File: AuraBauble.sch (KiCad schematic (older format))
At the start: 35 parts, among them J1 Bauble-Expando!, J2 USB_A, J3 SWD, SW1 KXT 321 LHS, U1 ATSAMD11D14A-M, U2 LP5912-3.3DRV, U3 74LVC1G02SE-7, Y1 FC-135R

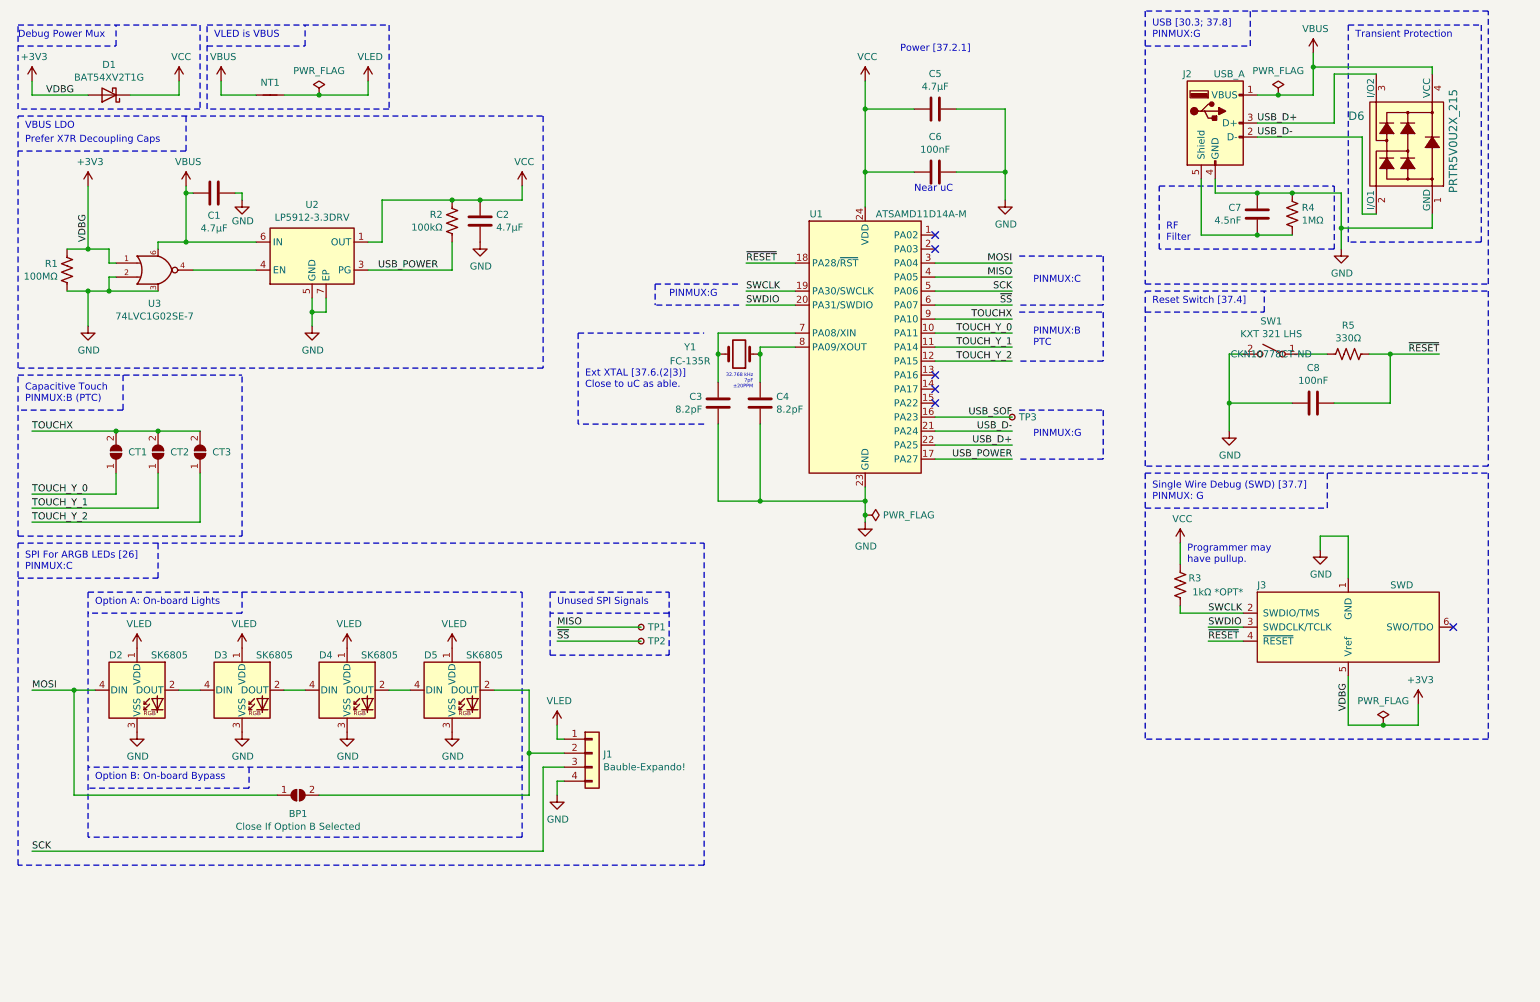
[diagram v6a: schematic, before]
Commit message: Closing in on a rev0.
I still think I need to level shift the SPI signals to the LEDs.
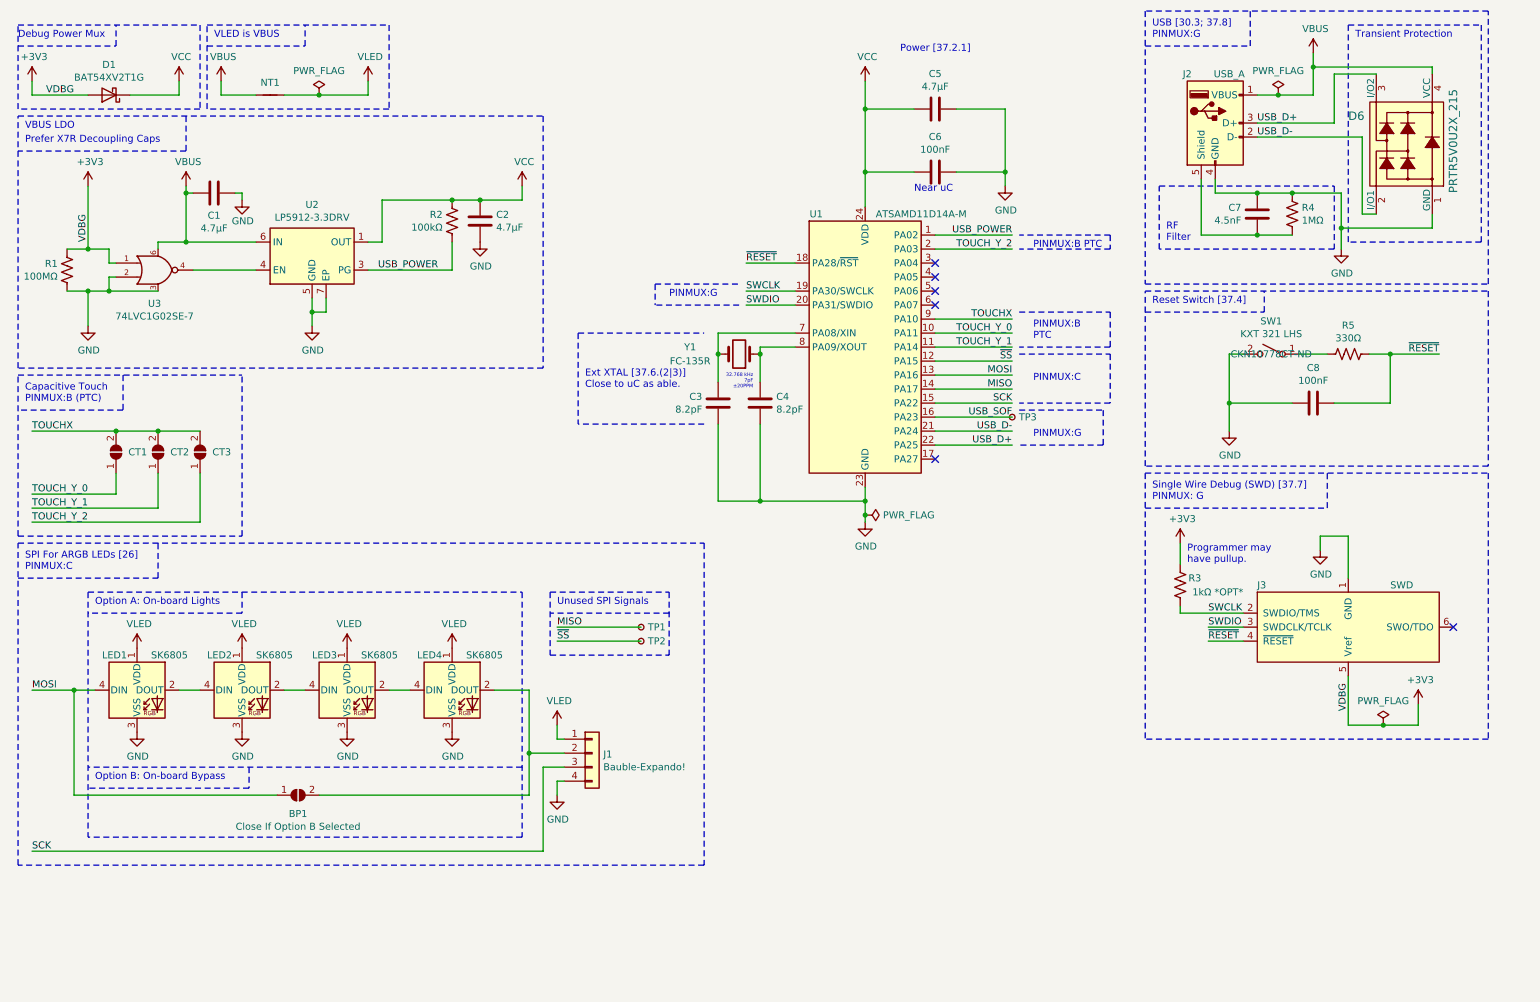
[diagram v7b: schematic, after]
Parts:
- J3: footprint Connector_DebugEdge:DebugEdge_2x05_Target -> Connector_DebugEdge:DebugEdge_2x03_Target
- renumbered D2 to LED1, D3 to LED2, D4 to LED3, D5 to LED4
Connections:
- net +3V3: now also R3.2
- net MISO: now also U1.14 (PA17); no longer U1.4 (PA05)
- net MOSI: now also U1.13 (PA16); no longer U1.3 (PA04)
- net SCK: now also U1.15 (PA22); no longer U1.5 (PA06)
- net TOUCH_Y_2: now also U1.2 (PA03); no longer U1.12 (PA15)
- net USB_POWER: now also U1.1 (PA02); no longer U1.17 (PA27)
- net VCC: no longer R3.2
- net ~SS~: now also U1.12 (PA15); no longer U1.6 (PA07)
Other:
- note added: "PINMUX:B PTC"
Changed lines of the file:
@@
 Near uC
 Wire Wire Line
-	7700 1650 7700 1850
+	7700 1650 7700 1750
 Connection ~ 7700 1650
 Wire Wire Line
@@
 L power:GND #PWR024
 U 1 1 5F5D1520
-P 7700 1850
-F 0 "#PWR024" H 7700 1600 50  0001 C CNN
-F 1 "GND" H 7705 1677 50  0000 C CNN
-F 2 "" H 7700 1850 50  0001 C CNN
-F 3 "" H 7700 1850 50  0001 C CNN
-	1    7700 1850
+P 7700 1750
+F 0 "#PWR024" H 7700 1500 50  0001 C CNN
+F 1 "GND" H 7705 1577 50  0000 C CNN
+F 2 "" H 7700 1750 50  0001 C CNN
+F 3 "" H 7700 1750 50  0001 C CNN
+	1    7700 1750
 	1    0    0    -1
 $EndComp
@@
 F 0 "J3" H 9500 5200 50  0000 L CNN
 F 1 "SWD" H 10450 5200 50  0000 L CNN
-F 2 "Connector_DebugEdge:DebugEdge_2x05_Target" H 10150 5300 50  0001 C CNN
+F 2 "Connector_DebugEdge:DebugEdge_2x03_Target" H 10150 5300 50  0001 C CNN
 F 3 "" H 10150 5300 50  0001 C CNN
 	1    10150 4900
@@
 	1    8950 4600
 	-1   0    0    1
-$EndComp
-$Comp
-L power:VCC #PWR025
-U 1 1 5F5E09D6
-P 8950 4300
-F 0 "#PWR025" H 8950 4150 50  0001 C CNN
-F 1 "VCC" H 8965 4473 50  0000 C CNN
-F 2 "" H 8950 4300 50  0001 C CNN
-F 3 "" H 8950 4300 50  0001 C CNN
-	1    8950 4300
-	1    0    0    -1
 $EndComp
 Wire Wire Line
@@
 $EndComp
 Wire Wire Line
-	7200 2300 7750 2300
-Wire Wire Line
-	7200 2400 7750 2400
-Wire Wire Line
-	7200 2500 7750 2500
-Wire Wire Line
-	7200 2600 7750 2600
-Text Label 7750 2300 2    50   ~ 0
+	7200 3100 7750 3100
+Wire Wire Line
+	7200 3200 7750 3200
+Wire Wire Line
+	7200 3300 7750 3300
+Wire Wire Line
+	7200 3000 7750 3000
+Text Label 7750 3100 2    50   ~ 0
 MOSI
-Text Label 7750 2400 2    50   ~ 0
+Text Label 7750 3200 2    50   ~ 0
 MISO
-Text Label 7750 2500 2    50   ~ 0
+Text Label 7750 3300 2    50   ~ 0
 SCK
-Text Label 7750 2600 2    50   ~ 0
+Text Label 7750 3000 2    50   ~ 0
 ~SS~
 Text Label 3650 2350 2    50   ~ 0
 USB_POWER
-Text Label 7750 3700 2    50   ~ 0
+Text Label 7750 2100 2    50   ~ 0
 USB_POWER
 Connection ~ 9650 1100
@@
 	1650 2500 1300 2500
 Connection ~ 1300 2500
-Text Notes 7900 2450 0    50   ~ 0
+Text Notes 7900 3150 0    50   ~ 0
 PINMUX:C
 Text Notes 7900 3550 0    50   ~ 0
 PINMUX:G
 Wire Notes Line
-	7800 2250 8400 2250
-Wire Notes Line
-	8400 2250 8400 2600
-Wire Notes Line
-	8400 2600 7800 2600
+	7800 2950 8450 2950
+Wire Notes Line
+	8450 2950 8450 3300
+Wire Notes Line
+	8450 3300 7800 3300
 Wire Notes Line
 	7800 3350 8400 3350
 Wire Notes Line
-	8400 3350 8400 3700
-Wire Notes Line
-	8400 3700 7800 3700
+	8400 3350 8400 3600
+Wire Notes Line
+	8400 3600 7800 3600
 Text Notes 4700 3200 0    50   ~ 0
 Ext XTAL [37.6.(2|3)]\nClose to uC as able.
@@
 Text Label 7750 2900 2    50   ~ 0
 TOUCH_Y_1
-Text Label 7750 3000 2    50   ~ 0
+Text Label 7750 2200 2    50   ~ 0
 TOUCH_Y_2
-Text Notes 7900 2900 0    50   ~ 0
+Text Notes 7900 2850 0    50   ~ 0
 PINMUX:B\nPTC
 Wire Notes Line
-	7800 2650 8400 2650
-Wire Notes Line
-	8400 2650 8400 3000
-Wire Notes Line
-	8400 3000 7800 3000
+	7800 2650 8450 2650
+Wire Notes Line
+	8450 2650 8450 2900
+Wire Notes Line
+	8450 2200 7800 2200
 Wire Wire Line
 	750  3950 1350 3950
@@
 ~SS~
 $Comp
-L LED:WS2812B D3
+L LED:WS2812B LED2
 U 1 1 5FB0FC37
 P 2250 5350
-F 0 "D3" H 2050 5600 50  0000 L CNN
+F 0 "LED2" H 2000 5600 50  0000 L CNN
 F 1 "SK6805" H 2350 5600 50  0000 L CNN
 F 2 "LED_SMD:LED_SK6812_EC15_1.5x1.5mm" H 2300 5050 50  0001 L TNN
@@
 $EndComp
 $Comp
-L LED:WS2812B D4
+L LED:WS2812B LED3
 U 1 1 5FB15975
 P 3000 5350
-F 0 "D4" H 2800 5600 50  0000 L CNN
+F 0 "LED3" H 2750 5600 50  0000 L CNN
 F 1 "SK6805" H 3100 5600 50  0000 L CNN
 F 2 "LED_SMD:LED_SK6812_EC15_1.5x1.5mm" H 3050 5050 50  0001 L TNN
@@
 $EndComp
 $Comp
-L LED:WS2812B D5
+L LED:WS2812B LED4
 U 1 1 5FB1BBDB
 P 3750 5350
-F 0 "D5" H 3550 5600 50  0000 L CNN
+F 0 "LED4" H 3500 5600 50  0000 L CNN
 F 1 "SK6805" H 3850 5600 50  0000 L CNN
 F 2 "LED_SMD:LED_SK6812_EC15_1.5x1.5mm" H 3800 5050 50  0001 L TNN
@@
 	1650 4550 1650 4300
 $Comp
-L LED:WS2812B D2
+L LED:WS2812B LED1
 U 1 1 5FABE3B5
 P 1500 5350
-F 0 "D2" H 1300 5600 50  0000 L CNN
+F 0 "LED1" H 1250 5600 50  0000 L CNN
 F 1 "SK6805" H 1600 5600 50  0000 L CNN
 F 2 "LED_SMD:LED_SK6812_EC15_1.5x1.5mm" H 1550 5050 50  0001 L TNN
@@
 	7200 3500 7750 3500
 Wire Wire Line
-	7200 3700 7750 3700
-Wire Wire Line
-	7200 3000 7750 3000
+	7200 2100 7750 2100
+Wire Wire Line
+	7200 2200 7750 2200
 Wire Wire Line
 	7200 2900 7750 2900
@@
 Wire Wire Line
 	6700 4000 6700 4100
-NoConn ~ 7200 3100
-NoConn ~ 7200 3200
-NoConn ~ 7200 3300
 Wire Wire Line
 	6200 2800 5650 2800
@@
 Wire Wire Line
 	7200 3400 7750 3400
-NoConn ~ 7200 2100
-NoConn ~ 7200 2200
 $Comp
 L Connector:TestPoint_Small TP3
@@
 	1    0    0    -1
 $EndComp
+$Comp
+L power:+3V3 #PWR0101
+U 1 1 5F705D10
+P 8950 4300
+F 0 "#PWR0101" H 8950 4150 50  0001 C CNN
+F 1 "+3V3" H 8965 4473 50  0000 C CNN
+F 2 "" H 8950 4300 50  0001 C CNN
+F 3 "" H 8950 4300 50  0001 C CNN
+	1    8950 4300
+	1    0    0    -1
+$EndComp
+Wire Notes Line
+	8450 2900 7800 2900
+Wire Notes Line
+	8450 2100 7800 2100
+Text Notes 7900 2200 0    50   ~ 0
+PINMUX:B PTC
+Wire Notes Line
+	8450 2100 8450 2200
+NoConn ~ 7200 3700
+NoConn ~ 7200 2600
+NoConn ~ 7200 2500
+NoConn ~ 7200 2400
+NoConn ~ 7200 2300
 $EndSCHEMATC

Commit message: Crammed a level shifter in, added fifth LED.
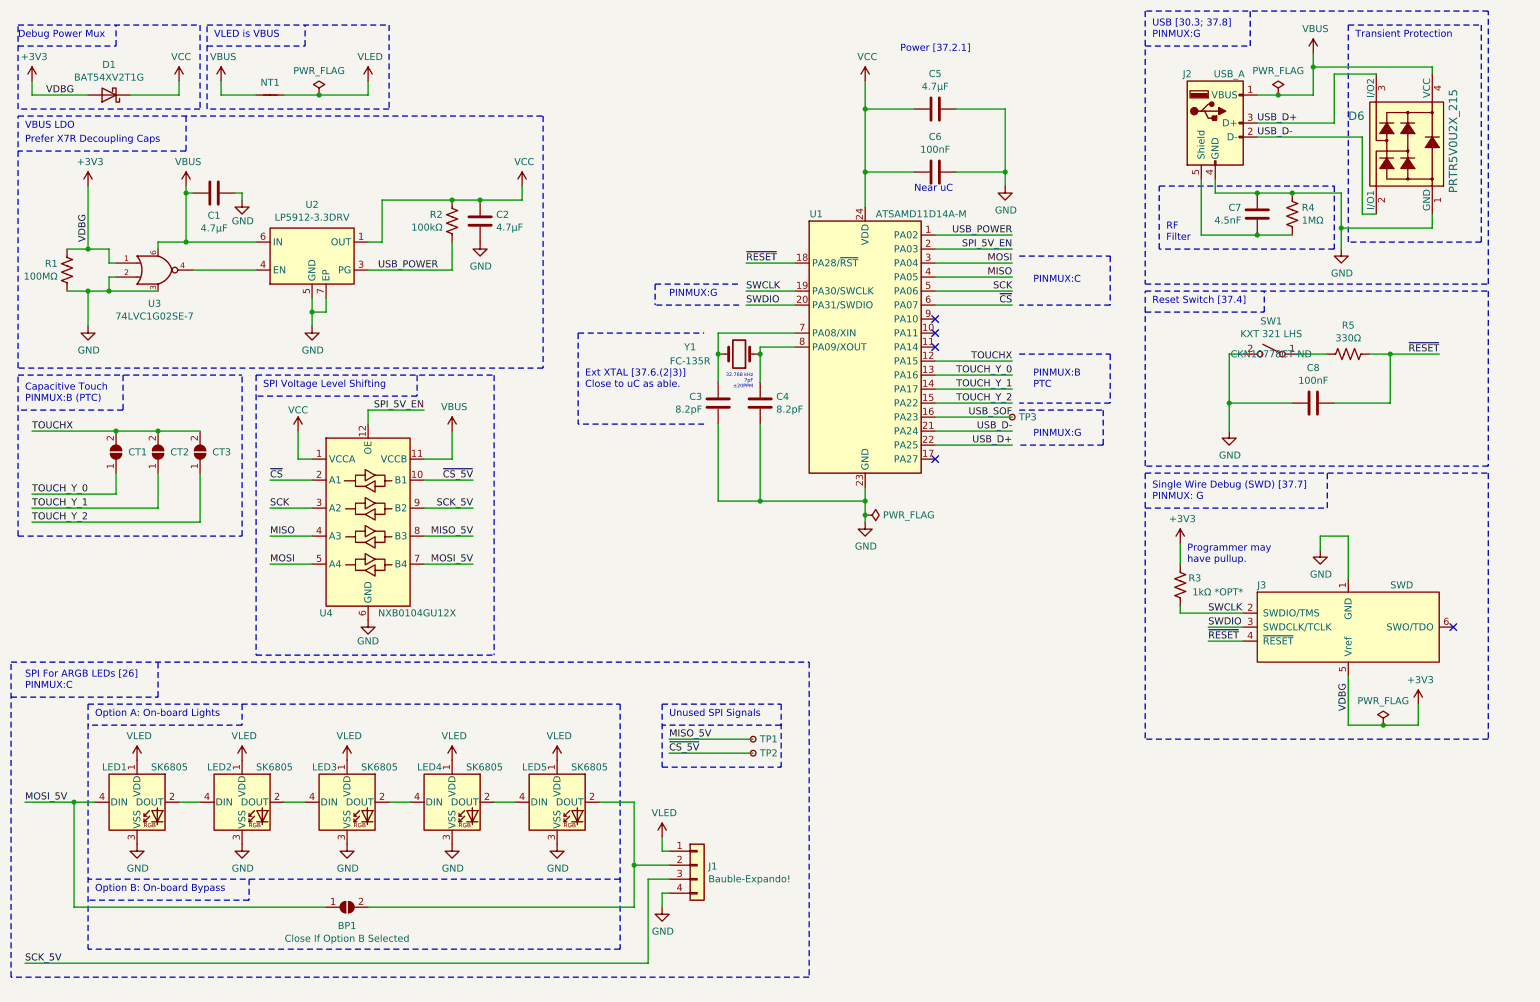
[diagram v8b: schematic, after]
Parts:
- added LED5: SK6805, LED_SMD:LED_SK6812_EC15_1.5x1.5mm, symbol LED:WS2812B
- added U4: NXB0104GU12X, AuraBauble:XQFN12, symbol AuraBauble_Custom:NXB0104GU12X
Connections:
- net GND: now also LED5.3 (VSS), U4.6 (GND)
- net MISO: now also U1.4 (PA05), U4.4 (A3); no longer TP1.1, U1.14 (PA17)
- net MOSI: now also U1.3 (PA04), U4.5 (A4); no longer BP1.1 (A), LED1.4 (DIN), U1.13 (PA16)
- net SCK: now also U1.5 (PA06), U4.3 (A2); no longer J1.3 (Pin_3), U1.15 (PA22)
- net TOUCHX: now also U1.12 (PA15); no longer U1.9 (PA10)
- net TOUCH_Y_0: now also U1.13 (PA16); no longer U1.10 (PA11)
- net TOUCH_Y_1: now also U1.14 (PA17); no longer U1.11 (PA14)
- net TOUCH_Y_2: now also U1.15 (PA22); no longer U1.2 (PA03)
- net VBUS: now also U4.11 (VCCB)
- net VCC: now also U4.1 (VCCA)
- net VLED: now also LED5.1 (VDD)
- net ~CS~: now reaches U1.6 (PA07)
- net ~CS~: now also U4.2 (A1)
- net at BP1.2 (B), J1.2 (Pin_2): now also LED5.2 (DOUT); no longer LED4.2 (DOUT)
- net ~SS~ renamed ~CS_5V~
- net ~CS_5V~: now also U4.10 (B1); no longer U1.12 (PA15)
- new net: LED4.2 (DOUT), LED5.4 (DIN)
- new net MISO_5V: TP1.1, U4.8 (B3)
- new net MOSI_5V: BP1.1 (A), LED1.4 (DIN), U4.7 (B4)
- new net SCK_5V: J1.3 (Pin_3), U4.9 (B2)
- new net SPI_5V_EN: U1.2 (PA03), U4.12 (OE)
- no-connect marks 6 -> 5
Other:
- note added: "SPI Voltage Level Shifting"
- note removed: "PINMUX:B PTC"
- moved on the sheet: BP1, J1, LED1, LED2, LED3, LED4, TP1, TP2
